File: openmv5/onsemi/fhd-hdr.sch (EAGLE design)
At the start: 58 parts, among them IC1 AP0202AT2L00XPGA0, IC2 MIC5365-2.8YC5-TR, IC3 TLV62568PDDCR, J1 DF12-36-DS, J2 DF12-36-DP, M1 9774030151R, M2 9774030151R, Q1 PMXB120EPEZ

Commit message: Add more cameras
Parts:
- removed J2: DF12-36-DP, DF12NB(3.0)-36DP-0.5V(51):DF12-36-DP
- removed M1, M2: 9774030151R, 9774030151R:9774030151R
- removed R5: 100K, rcl:R-US_R0402
- removed R6: 10K, rcl:R-US_R0402
- added C30, C31, C34, C46, C47: 4.7uF, 0402:CAP_0402
- added C32, C33, C35, C37, C38, C39, C40, C41, C42, C43, C44, C45: 0.22uF, rcl:C-EUC0201
- added C36, C48, C49: 22uF, SparkFun-Capacitors:22UF-0805-6.3V-20%
- added H1: LENSMOUNT20MM, lensmount:LENSMOUNT20MM
- added L8: 100, 0402:INDUCTOR_0402
- C1, C8: value 0.22uF -> 4.7uF; device rcl:C-EUC0201 -> 0402:CAP_0402; MPN GRM033R60J224ME15D -> JMK105BBJ475MV-F
- C15: value 4.7uF -> 22uF; device 0402:CAP_0402 -> SparkFun-Capacitors:22UF-0805-6.3V-20%; MPN JMK105BBJ475MV-F -> CL21A226MQQNNNE
- C18, C19, C20, C21, C22, C23: value 4.7uF -> 0.22uF; device 0402:CAP_0402 -> rcl:C-EUC0201; MPN JMK105BBJ475MV-F -> GRM033R60J224ME15D
- C2, C9: value 0.22uF -> 22uF; device rcl:C-EUC0201 -> SparkFun-Capacitors:22UF-0805-6.3V-20%; MPN GRM033R60J224ME15D -> CL21A226MQQNNNE
- C24, C27, C28, C29: value 22uF -> 0.22uF; device SparkFun-Capacitors:22UF-0805-6.3V-20% -> rcl:C-EUC0201; MPN CL21A226MQQNNNE -> GRM033R60J224ME15D
- C25: value 22uF -> 4.7uF; device SparkFun-Capacitors:22UF-0805-6.3V-20% -> 0402:CAP_0402; MPN CL21A226MQQNNNE -> JMK105BBJ475MV-F
- IC1: value AP0202AT2L00XPGA0 -> AR0231AT7C00XUEA0-DRBR-E; device AP0202AT2L00XPGA0:AP0202AT2L00XPGA0 -> AR0231AT7C00XUEA0-DRBR-E:AR0231AT7C00XUEA0-DRBR-E; MPN AP0202AT2L00XPGA0-DR -> AR0231AT7C00XUEA0-DPBR
- IC2: value MIC5365-2.8YC5-TR -> TLV62568PDDCR; device MIC5365-2.8YC5-TR:MIC5365-2.8YC5-TR -> TLV62568PDDCR:TLV62568PDDCR; MPN MIC5365-2.8YC5-TR -> TLV62568PDDCR
- IC3: value TLV62568PDDCR -> MIC5365-2.8YC5-TR; device TLV62568PDDCR:TLV62568PDDCR -> MIC5365-2.8YC5-TR:MIC5365-2.8YC5-TR; MPN TLV62568PDDCR -> MIC5365-2.8YC5-TR
- J1: value DF12-36-DS -> DF12-36-DP; device DF12-36-DS:DF12-36-DS -> DF12NB(3.0)-36DP-0.5V(51):DF12-36-DP; MPN DF12NB-36DS-0.5V(51) -> DF12NB(3.0)-36DP-0.5V(51)
- L1: value MAKK2016T2R2M -> 100; device MAKK2016T2R2M:MAKK2016T2R2M -> 0402:INDUCTOR_0402; MPN MAKK2016T2R2M -> MFBM1V1005-101-R
- L4: value 100 -> MAKK2016T2R2M; device 0402:INDUCTOR_0402 -> MAKK2016T2R2M:MAKK2016T2R2M; MPN MFBM1V1005-101-R -> MAKK2016T2R2M
- R1, R2: value 1.5K -> 100K; MPN RC0402FR-131K5L -> AC0402FR-07100KL
- R3: value 100K -> 10K; MPN AC0402FR-07100KL -> AC0402FR-1310KL
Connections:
- removed net DCMI_MISO: J1.15, J2.15
- removed net DCMI_MOSI: J1.17, J2.17
- removed net DCMI_SCLK: J1.13, J2.13
- removed net DCMI_SSEL: J1.11, J2.11
- removed net SENSOR_CLK: IC1.EXT_CLK_OUT, J1.12
- removed net SENSOR_D0: IC1.DIN_0, J1.3
- removed net SENSOR_D1: IC1.DIN_1, J1.1
- removed net SENSOR_D10: IC1.DIN_10, J1.24
- removed net SENSOR_D11: IC1.DIN_11, J1.22
- removed net SENSOR_D12: J1.8
- removed net SENSOR_D2: IC1.DIN_2, J1.9
- removed net SENSOR_D3: IC1.DIN_3, J1.7
- removed net SENSOR_D4: IC1.DIN_4, J1.31
- removed net SENSOR_D5: IC1.DIN_5, J1.29
- removed net SENSOR_D6: IC1.DIN_6, J1.35
- removed net SENSOR_D7: IC1.DIN_7, J1.28
- removed net SENSOR_D8: IC1.DIN_8, J1.26
- removed net SENSOR_D9: IC1.DIN_9, J1.33
- removed net SENSOR_FSIN: IC1.TRIGGER_OUT/GPIO_0, J1.23
- removed net SENSOR_HSYNC: IC1.LV_IN, J1.18
- removed net SENSOR_PCLK: IC1.PIXCLK_IN, J1.14
- removed net SENSOR_RST: IC1.RESET_N_OUT, J1.21
- removed net SENSOR_SCL: IC1.M_SCLK, J1.32, R1.1
- removed net SENSOR_SDA: IC1.M_SDATA, J1.34, R2.1
- removed net SENSOR_VSYNC: IC1.FV_IN, J1.16
- removed net SENSOS_D13: J1.6
- removed net VDDIO_H: C13.2, C19.2, C2.2, C25.2, C3.2, C4.2, IC1.EXT_REG, IC1.SADDR, IC1.VDDIO_H0, IC1.VDDIO_H1, IC1.VDDIO_H2, IC1.VDD_REG, L3.P$1
- removed net VDDIO_OTPM: C10.2, C18.2, C24.2, IC1.VDDIO_OTPM, L2.P$1
- removed net VDDIO_S: C1.2, C20.2, C26.2, IC1.VDDIO_S, L4.P$1
- removed net VDD_PLL: C22.2, C28.2, C5.2, IC1.VDD_PLL, L6.P$1
- new net DCMI_D10: IC1.DOUT10, J1.24
- new net DCMI_D11: IC1.DOUT11, J1.22
- new net DCMI_D12: IC1.DOUT12, J1.8
- new net DCMI_D13: IC1.DOUT13, J1.6
- new net DCMI_D8: IC1.DOUT8, J1.26
- new net DCMI_D9: IC1.DOUT9, J1.33
- new net SPI_MISO: J1.15
- new net SPI_MOSI: J1.17
- new net SPI_SCLK: J1.13
- new net SPI_SSEL: J1.11
- new net VAA: C19.1, C29.1, C34.2, C36.2, C38.1, C40.1, C6.2, IC1.VAA_1, IC1.VAA_2, IC1.VAA_3, IC1.VAA_4, IC1.VAA_5, L6.P$1
- new net VAA_PIX: C32.1, C46.2, C48.2, IC1.VAA_PIX, L7.P$1
- new net VDDIO: C10.1, C13.2, C20.2, C24.1, C3.1, C33.2, C37.2, C42.2, C45.2, C47.2, C49.2, C7.1, IC1.VDD_IO_1, IC1.VDD_IO_10, IC1.VDD_IO_2, IC1.VDD_IO_3, IC1.VDD_IO_4, IC1.VDD_IO_5, IC1.VDD_IO_6, IC1.VDD_IO_7, IC1.VDD_IO_8, IC1.VDD_IO_9, L8.P$1
- new net VDD_IO_PHY: C23.1, C25.2, C26.2, IC1.VDD_IO_PHY, L5.P$1
- new net VDD_SLVS: C16.2, C17.2, C21.1, IC1.VDD_SLVS, L3.P$1
- net DCMI_CLK: now also J1.12; no longer J2.12
- net DCMI_D0: now also IC1.DOUT0, J1.3; no longer IC1.DOUT_16, J2.31
- net DCMI_D1: now also IC1.DOUT1, J1.1; no longer IC1.DOUT_17, J2.29
- net DCMI_D2: now also IC1.DOUT2, J1.9; no longer IC1.DOUT_18, J2.35
- net DCMI_D3: now also IC1.DOUT3, J1.7; no longer IC1.DOUT_19, J2.28
- net DCMI_D4: now also IC1.DOUT4, J1.31; no longer IC1.DOUT_20, J2.26
- net DCMI_D5: now also IC1.DOUT5, J1.29; no longer IC1.DOUT_21, J2.33
- net DCMI_D6: now also IC1.DOUT6, J1.35; no longer IC1.DOUT_22, J2.24
- net DCMI_D7: now also IC1.DOUT7, J1.28; no longer IC1.DOUT_23, J2.22
- net DCMI_FSIN: now also IC1.GPIO3, J1.23; no longer IC1.FRAME_SYNC, J2.23
- net DCMI_HSYNC: now also IC1.FRAME_VALID, J1.18; no longer IC1.LV_OUT, J2.18
- net DCMI_PCLK: now also IC1.PIXCLK, J1.14; no longer IC1.PIXCLK_OUT, J2.14
- net DCMI_PWDN: no longer IC1.STANDBY, J2.25
- net DCMI_PWDN_INT: now also IC3.EN, R4.1; no longer IC2.EN, R5.1
- net DCMI_RST: now also J1.21, R3.2; no longer J2.21, R6.2
- net DCMI_SCL: now also J1.32; no longer J2.32
- net DCMI_SDA: now also J1.34; no longer J2.34
- net DCMI_VSYNC: now also IC1.LINE_VALID, J1.16; no longer IC1.FV_OUT, J2.16
- net FB: now also IC2.FB, R1.1, R2.1; no longer IC3.FB, R3.1, R4.1
- net GND: now also C10.2, C11.2, C18.2, C19.2, C21.2, C22.2, C23.2, C24.2, C29.2, C3.2, C30.1, C31.1, C32.2, C33.1, C34.1, C35.1, C36.1, C37.1, C38.2, C39.1, C4.2, C40.2, C41.2, C42.1, C43.1, C44.1, C45.1, C46.1, C47.1, C48.1, C49.1, C5.2, C7.2, IC1.AGND_1, IC1.AGND_2, IC1.AGND_3, IC1.AGND_4, IC1.AGND_5, IC1.DGND_1, IC1.DGND_10, IC1.DGND_11, IC1.DGND_12, IC1.DGND_13, IC1.DGND_14, IC1.DGND_15, IC1.DGND_16, IC1.DGND_17, IC1.DGND_18, IC1.DGND_19, IC1.DGND_2, IC1.DGND_20, IC1.DGND_21, IC1.DGND_22, IC1.DGND_23, IC1.DGND_24, IC1.DGND_25, IC1.DGND_26, IC1.DGND_27, IC1.DGND_28, IC1.DGND_29, IC1.DGND_3, IC1.DGND_30, IC1.DGND_31, IC1.DGND_32, IC1.DGND_33, IC1.DGND_34, IC1.DGND_35, IC1.DGND_36, IC1.DGND_37, IC1.DGND_38, IC1.DGND_39, IC1.DGND_4, IC1.DGND_40, IC1.DGND_5, IC1.DGND_6, IC1.DGND_7, IC1.DGND_8, IC1.DGND_9, IC1.SADDR0, IC1.SADDR1, IC1.SADDR2, R2.2; no longer C10.1, C11.1, C18.1, C19.1, C21.1, C22.1, C23.1, C24.1, C29.1, C3.1, C4.1, C5.1, C7.1, IC1.DGND, IC1.ENDLO, IC1.GND0, IC1.GND1, IC1.GND2, IC1.GND3, IC1.GND4, IC1.GND5, IC1.GND6, IC1.GND7, IC1.HISPI0N, IC1.HISPI0P, IC1.HISPI1N, IC1.HISPI1P, IC1.HISPICN, IC1.HISPICP, IC1.RESERVED_0, IC1.RESERVED_1, IC1.SPI_SDI, J2.19, J2.27, J2.5, R5.2
- net RESET_N: now also IC1.RESET_BAR, IC2.PG, R3.1; no longer IC1.RESET_N, IC3.PG, R6.1
- net SW: now also IC2.SW, L4.2; no longer IC3.SW, L1.2
- net VCC: now also C14.2; no longer C15.2, C16.2, IC3.VIN, J2.10, J2.2, J2.20, J2.30, J2.36, L2.P$2, L3.P$2, Q1.S, R1.2, R2.2
- net VDD: now also C1.2, C11.1, C18.1, C2.2, C27.2, C28.2, C35.2, C39.2, C4.1, C41.1, C43.2, C44.2, C5.1, IC1.VDD_1, IC1.VDD_10, IC1.VDD_11, IC1.VDD_2, IC1.VDD_3, IC1.VDD_4, IC1.VDD_5, IC1.VDD_6, IC1.VDD_7, IC1.VDD_8, IC1.VDD_9, L1.P$1; no longer C23.2, C29.2, C6.2, C7.2, C8.2, C9.2, IC1.VDD0, IC1.VDD1, IC1.VDD2, IC1.VDD3, L7.P$1
- net VDDA: now also C31.2, IC3.VIN, Q1.S; no longer J2.4
- net VDDIO_REG: now also C30.2, IC2.EN, IC3.VOUT, L6.P$2, L7.P$2, L8.P$2; no longer C14.2, IC2.VOUT, IC3.EN, L4.P$2
- net VDD_PHY: now also C22.1, C8.2, C9.2, L2.P$1; no longer C11.2, C21.2, C27.2, L5.P$1
- net VDD_REG: now also C15.2, L1.P$2, L2.P$2, L3.P$2, L4.1, R1.2; no longer C17.2, L1.1, L6.P$2, L7.P$2, R3.2
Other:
- note added: "Camera Sensor"
- note added: "Connector"
- note removed: "Host Connector"
- note removed: "ISP"
- note removed: "SENSOR CONNECTOR"
- moved on the sheet: C1, C10, C11, C12, C13, C14, C15, C16, C17, C18, C19, C2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

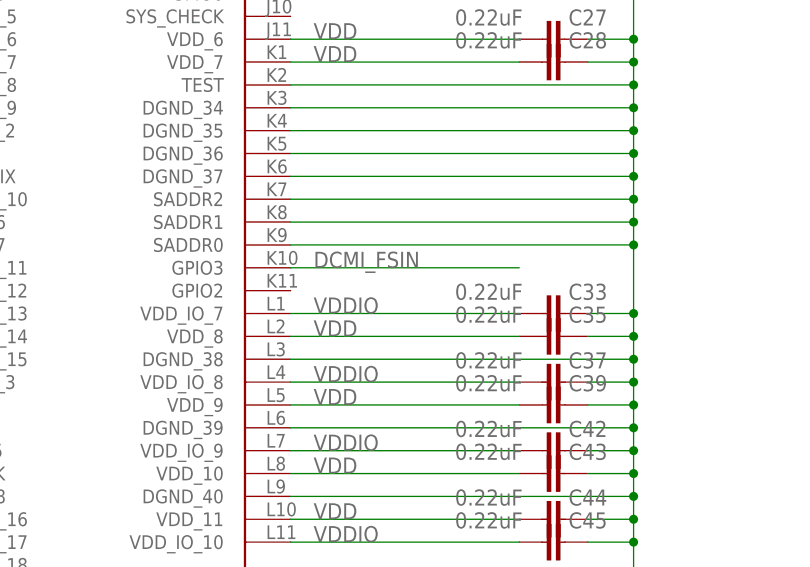
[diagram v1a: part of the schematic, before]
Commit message: Finish out new onsemi cameras
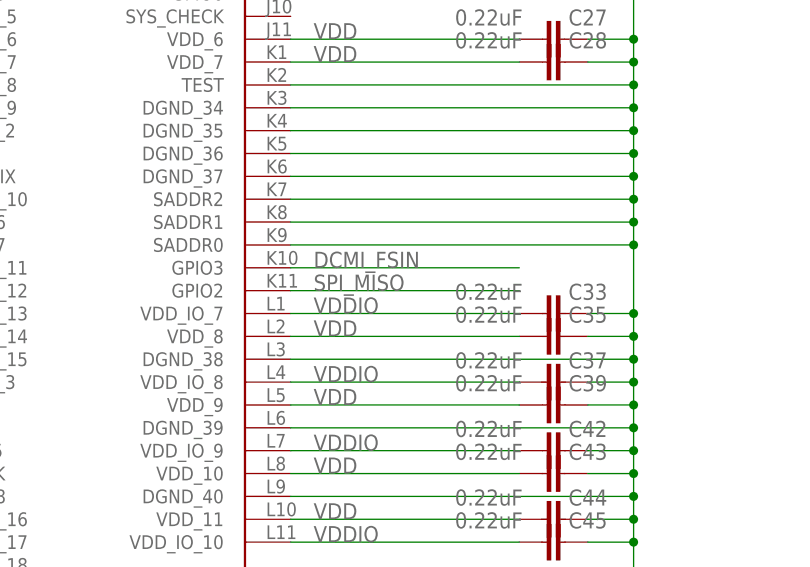
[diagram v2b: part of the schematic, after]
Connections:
- net SPI_MISO: now also IC1.GPIO2
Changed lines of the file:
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@@
 <pinref part="J1" gate="G$1" pin="15"/>
+</segment>
+<segment>
+<pinref part="IC1" gate="G$1" pin="GPIO2"/>
+<wire x1="99.06" y1="104.14" x2="124.46" y2="104.14" width="0.1524" layer="91"/>
+<label x="101.6" y="104.14" size="1.778" layer="95"/>
 </segment>
 </net>

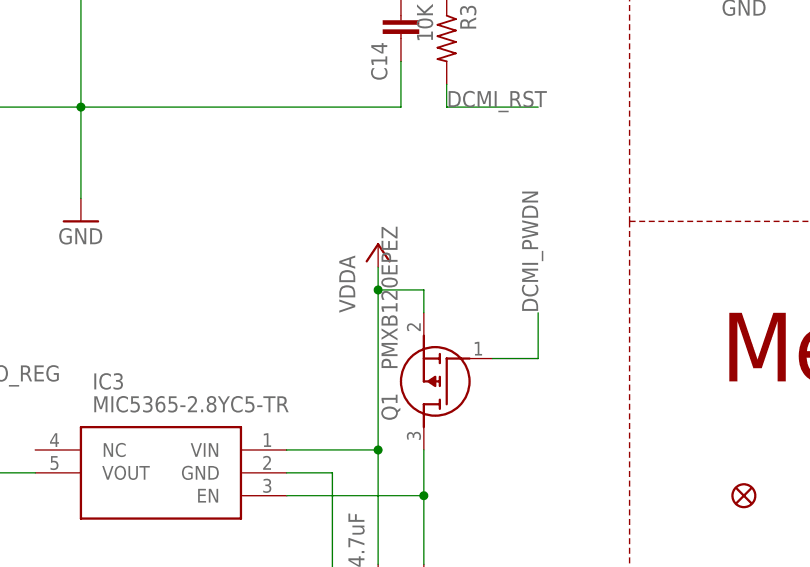
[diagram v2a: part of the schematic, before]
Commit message: Update camera modules to use different non-flippable pmosfet
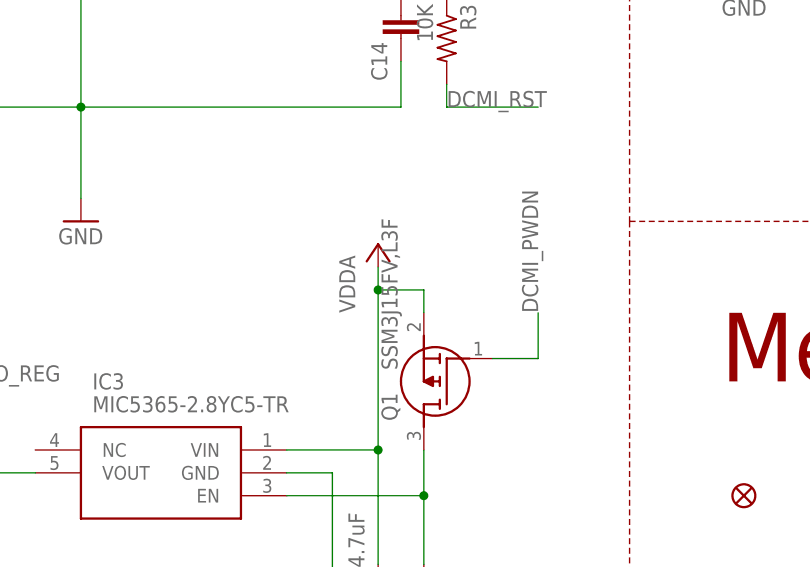
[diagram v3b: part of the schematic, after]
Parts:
- Q1: value PMXB120EPEZ -> SSM3J15FV,L3F; device PMXB120EPEZ:PMXB120EPEZ -> SSM3J15FV_L3F:SSM3J15FV,L3F; MPN PMXB120EPEZ -> SSM3J15FV,L3F
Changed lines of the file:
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@@
 </part>
 <part name="GND11" library="supply" deviceset="GND" device=""/>
-<part name="Q1" library="PMXB120EPEZ" deviceset="PMXB120EPEZ" device="">
-<attribute name="MPN" value="PMXB120EPEZ"/>
+<part name="Q1" library="SSM3J15FV_L3F" deviceset="SSM3J15FV,L3F" device="">
+<attribute name="MPN" value="SSM3J15FV,L3F"/>
 </part>
 <part name="R4" library="rcl" library_urn="urn:adsk.eagle:library:334" deviceset="R-US_" device="R0402" package3d_urn="urn:adsk.eagle:package:23547/3" value="100K">
